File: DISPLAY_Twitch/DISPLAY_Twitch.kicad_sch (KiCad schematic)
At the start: 60 parts, among them J1 Conn_01x06_Pin, J2 Conn_01x06_Pin, Q1 Q_PNP_BEC, Q2 Q_PNP_BEC, Q3 Q_PNP_BEC, Q4 Q_PMOS_GSD, Q5 Q_PMOS_GSD, Q6 Q_PNP_BEC, Q7 Q_PNP_BEC, Q8 Q_PMOS_GSD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

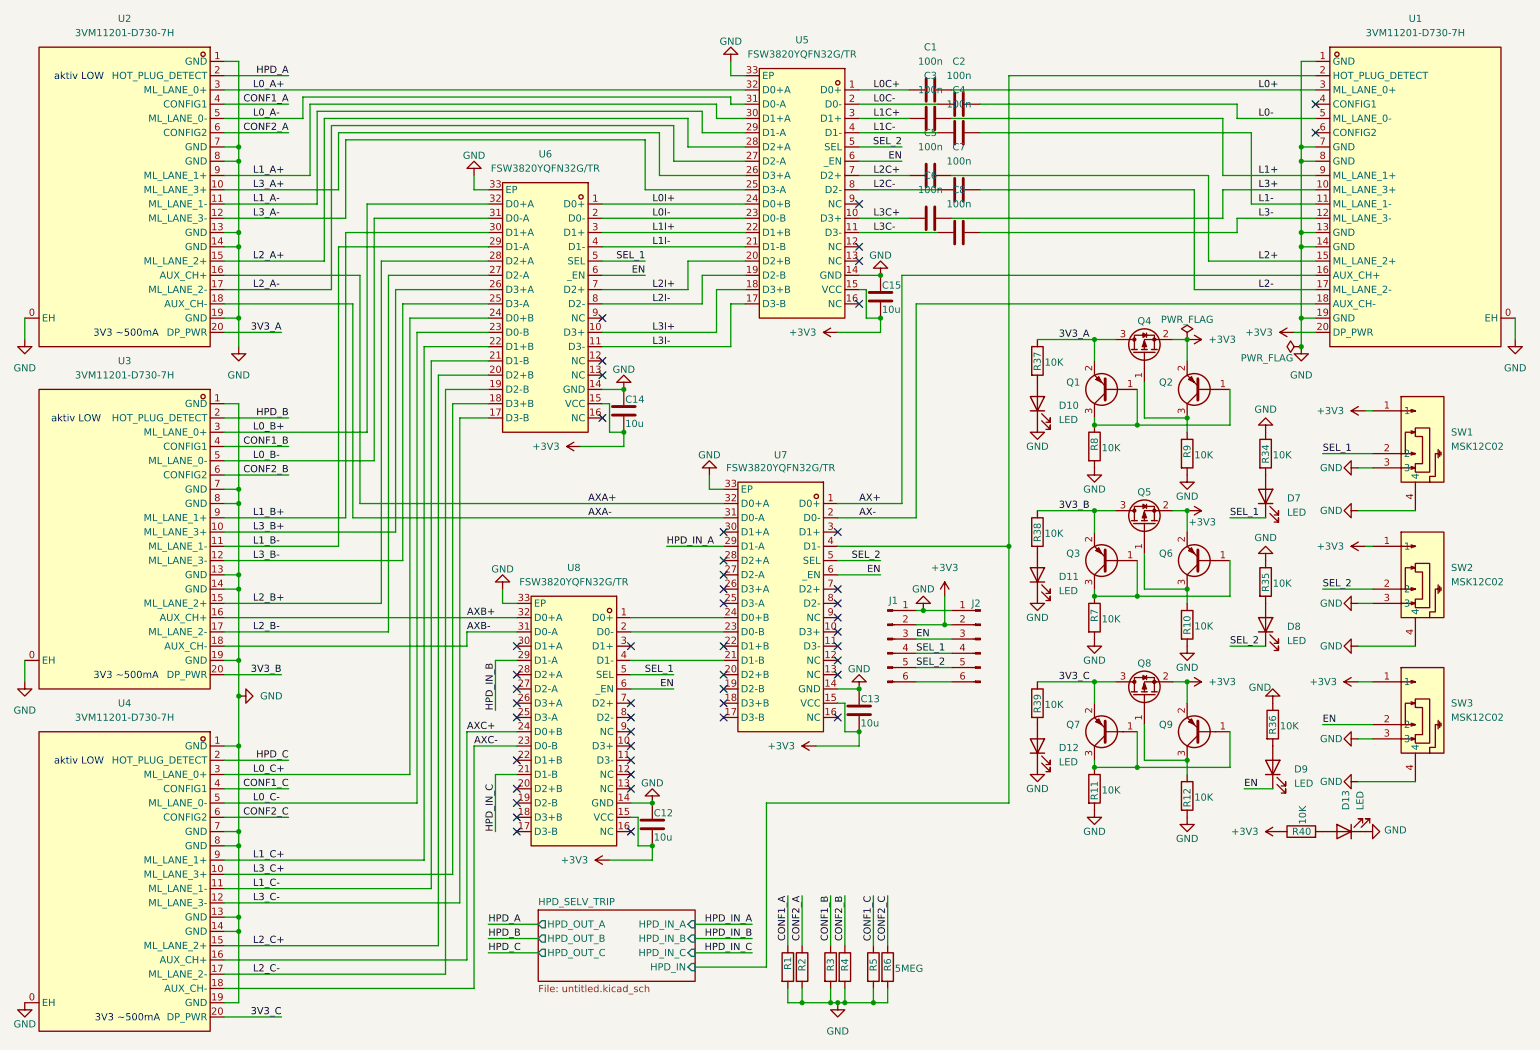
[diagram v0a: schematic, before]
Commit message: add nev versions. (usb c and displayport working)
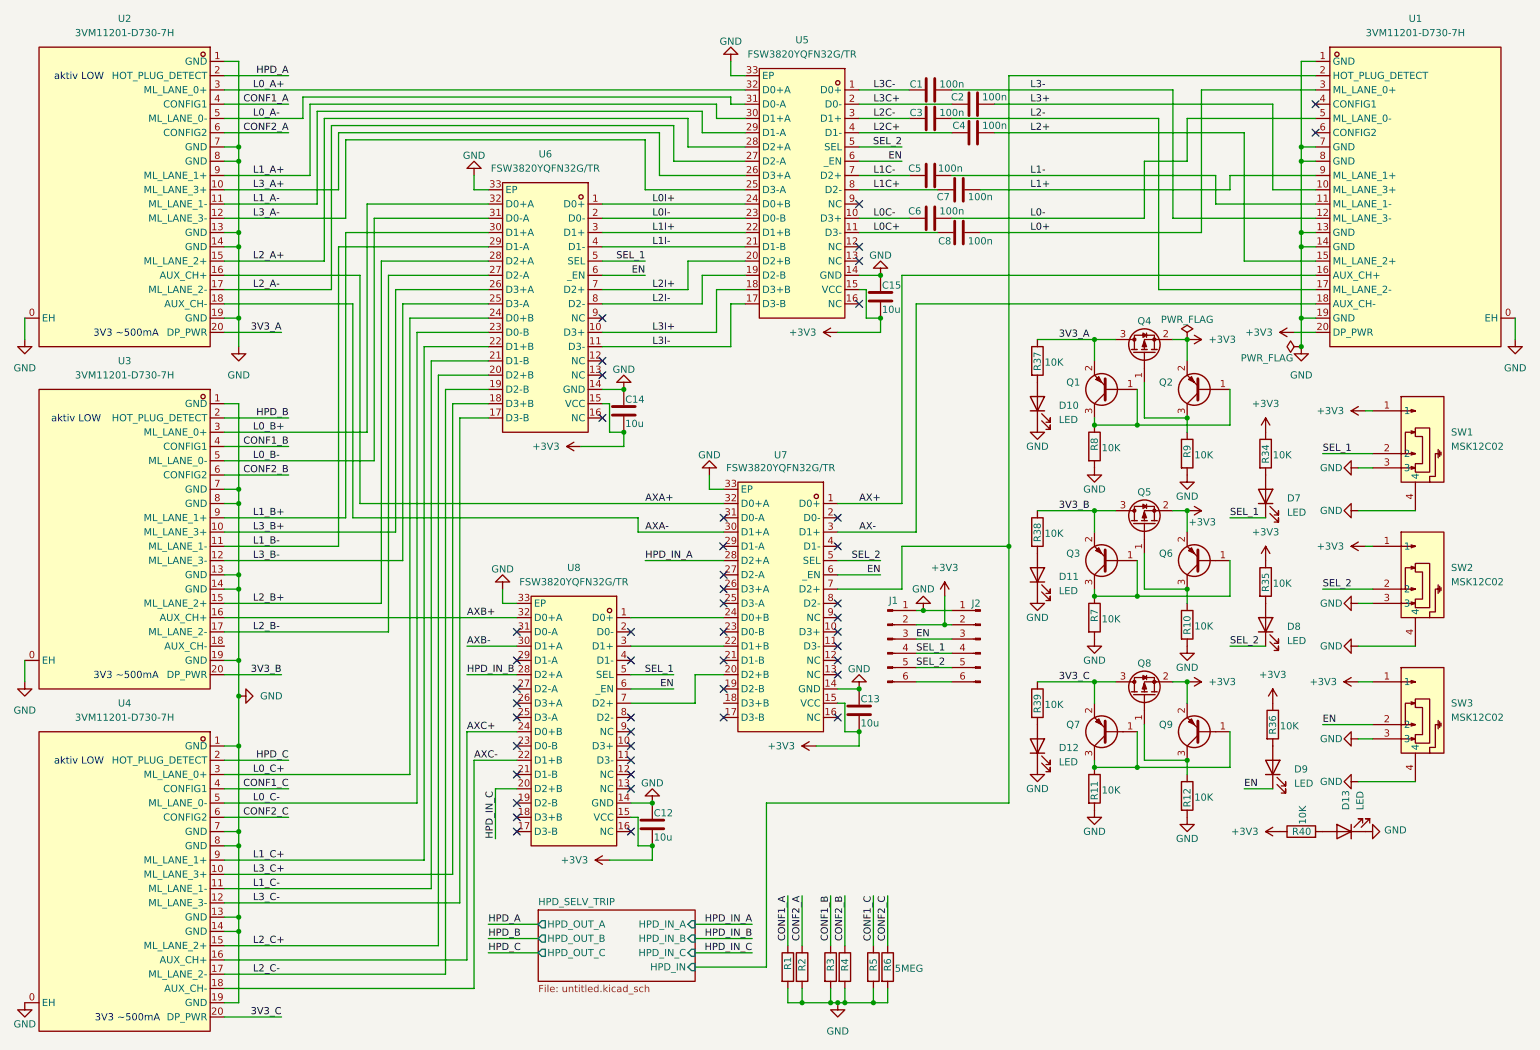
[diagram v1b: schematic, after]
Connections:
- net +3V3: now also R34.1, R35.1, R36.1
- net AX-: now also U7.3 (D1+); no longer U7.2 (D0-)
- net AXA-: now also U7.30 (D1+A); no longer U7.31 (D0-A)
- net AXB-: now also U8.30 (D1+A); no longer U3.18 (AUX_CH-), U8.31 (D0-A)
- net AXC-: now also U8.22 (D1+B); no longer U8.23 (D0-B)
- net GND: no longer R34.1, R35.1, R36.1
- net HPD_IN_A: now also U7.28 (D2+A); no longer U7.29 (D1-A)
- net HPD_IN_B: now also U8.28 (D2+A); no longer U8.29 (D1-A)
- net HPD_IN_C: now also U8.20 (D2+B); no longer U8.21 (D1-B)
- net HPD_SELV_TRIP/HPD_IN: now also U7.7 (D2+); no longer U7.4 (D1-)
- net L0+: now also C8.2; no longer C1.2
- net L0-: now also C6.2; no longer C2.2
- net L0C+: now also C8.1, U5.11 (D3-); no longer C1.1, U5.1 (D0+)
- net L0C-: now also C6.1, U5.10 (D3+); no longer C2.1, U5.2 (D0-)
- net L1+: now also C7.2; no longer C3.2
- net L1-: now also C5.2; no longer C4.2
- net L1C+: now also C7.1, U5.8 (D2-); no longer C3.1, U5.3 (D1+)
- net L1C-: now also C5.1, U5.7 (D2+); no longer C4.1, U5.4 (D1-)
- net L2+: now also C4.2; no longer C5.2
- net L2-: now also C3.2; no longer C7.2
- net L2C+: now also C4.1, U5.4 (D1-); no longer C5.1, U5.7 (D2+)
- net L2C-: now also C3.1, U5.3 (D1+); no longer C7.1, U5.8 (D2-)
- net L3+: now also C2.2; no longer C6.2
- net L3-: now also C1.2; no longer C8.2
- net L3C+: now also C2.1, U5.2 (D0-); no longer C6.1, U5.10 (D3+)
- net L3C-: now also C1.1, U5.1 (D0+); no longer C8.1, U5.11 (D3-)
- net at U7.20 (D2+B): now also U8.7 (D2+)
- net at U7.21 (D1-B): no longer U8.4 (D1-)
- net at U7.22 (D1+B): now also U8.3 (D1+)
- net at U7.23 (D0-B): no longer U8.2 (D0-)
- no-connect marks 48 -> 47
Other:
- moved on the sheet: C2, C4
